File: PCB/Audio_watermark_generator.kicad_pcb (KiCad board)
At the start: 4 copper layers, 83 x 41 mm, 85 parts, among them IC1 STM32G431KBT6, IC2 ISL91107IRTNZ-T7A, J1 USB_B_Micro, J2 Conn_01x03, J3 Conn_01x04_Pin, J4 SJ2-35954A-SMT-TR, J5 SJ2-35954A-SMT-TR, J6 533980271_Picoblade, J7 CONSMA002-SMD-G-T, J8 Conn_01x01_Pin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

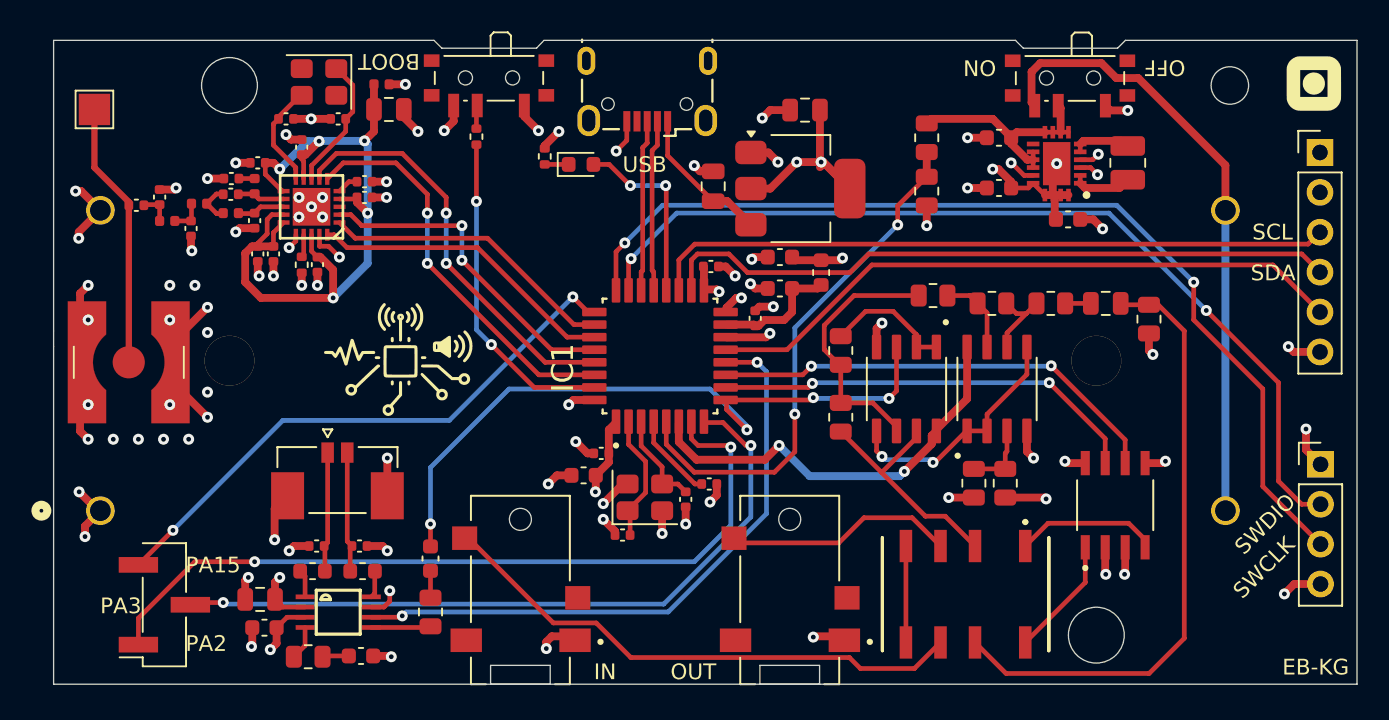
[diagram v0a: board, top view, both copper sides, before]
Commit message: Update PCB settings and Gerber files for Audio Watermark Generator (#122)
* Update PCB settings and add new VIP net class

* Update Gerber files for Audio Watermark Generator

- Updated creation timestamps in NPTH and PTH drill files to reflect the latest generation time.
- Modified aperture sizes in the PTH drill file for improved accuracy.
- Added a new User Eco layer file (Audio_watermark_generator-User_Eco1.gbr) with detailed aperture and coordinate definitions.
- Updated job file (Audio_watermark_generator-job.gbrjob) to include the new User Eco layer and updated creation date.

* Update Gerber files and creation dates for Audio Watermark Generator project

- Updated creation dates in all Gerber files to reflect the new timestamp of 2026-03-25T20:04:04+01:00.
- Added new Gerber files: Audio_watermark_generator-gm6.gbr and Audio_watermark_generator-gm7.gbr.
- Modified drill files (NPTH and PTH) to update creation dates.
- Updated job file to include new creation date and added references for new Gerber files.
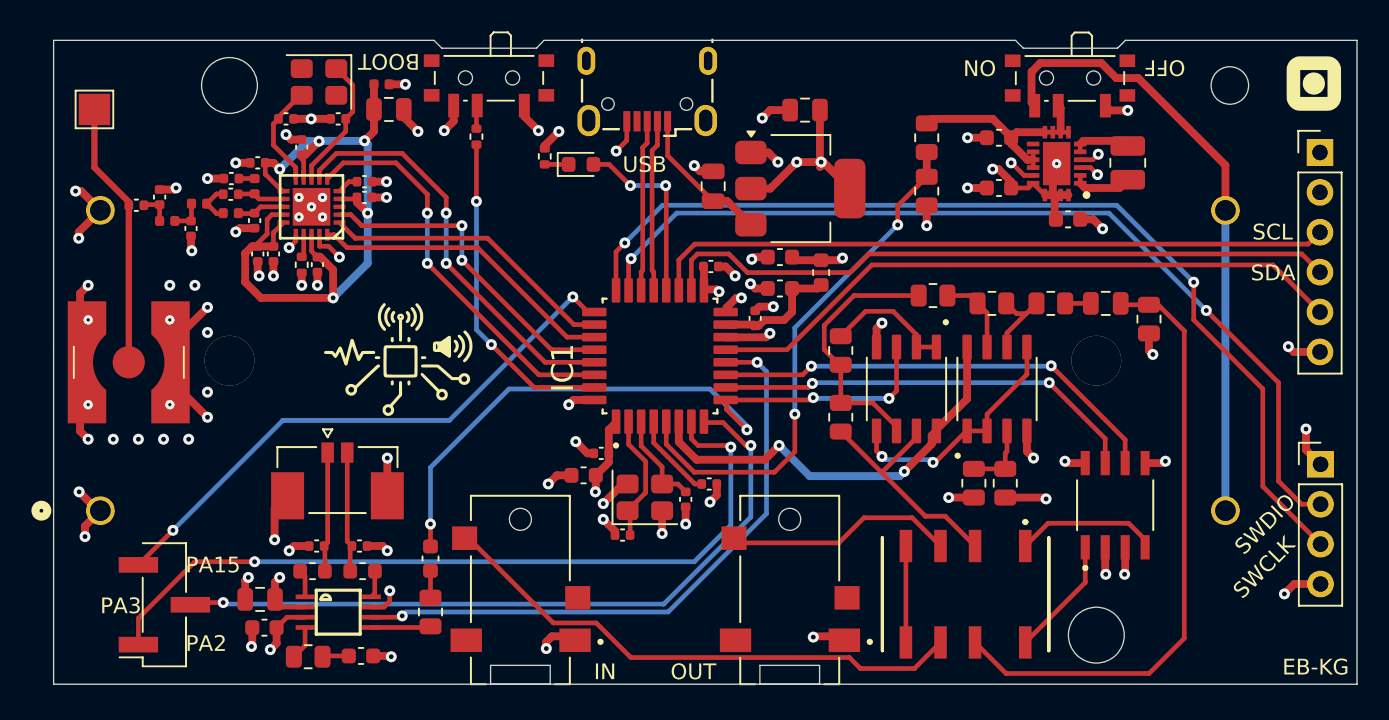
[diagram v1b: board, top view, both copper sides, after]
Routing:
- net GND: track 122.1 -> 121.4 mm
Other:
- board text added: "VIA IN PAD - CAPPED"
- board text added: "VIA IN PAD - EPOXY FILLED"
